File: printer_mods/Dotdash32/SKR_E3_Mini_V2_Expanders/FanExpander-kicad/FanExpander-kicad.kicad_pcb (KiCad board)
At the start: 2 copper layers, 46.3 x 37.3 mm, 69 parts, among them J0 FAN0, J1 FAN1, J10 FAN0_IN, J12 HI_PWR_IN, J2 FAN2, J3 FAN3, J4 FAN4, J5 FAN5, J6 FAN6, J7 FAN7, J8 EXP1_IN, J9 5V_In, Q1 IRLML6344, Q2 IRLML6344, Q3 IRLML6344, Q4 IRLML6344, Q5 IRLML6344, Q6 IRLML6344, Q7 IRLML6344

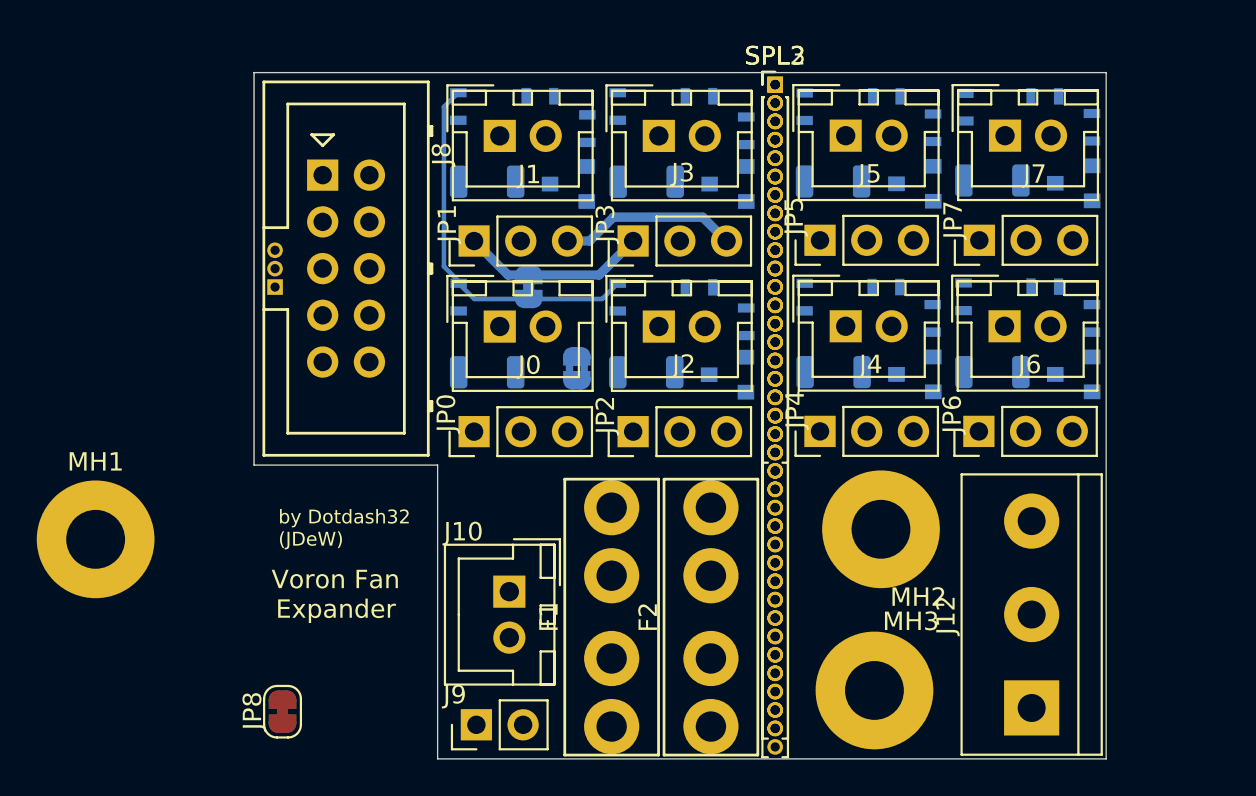
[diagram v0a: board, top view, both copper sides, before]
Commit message: feat: new layout with screw terminals and jumpers
add more jumpers to make any kind of voltage selection more easy,
particularly for fan0, either always on or cutting 24V in

no routing done yet lol
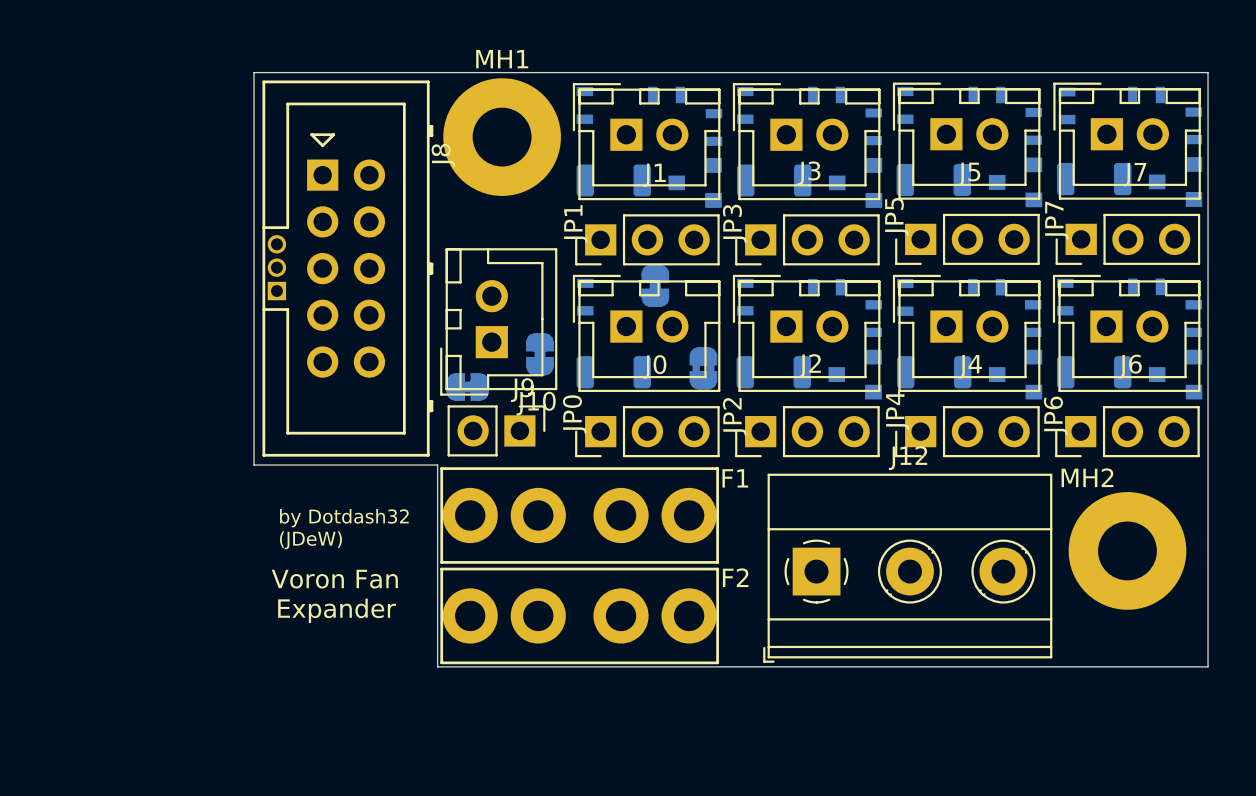
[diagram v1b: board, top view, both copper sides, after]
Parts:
- removed MH3: MountingHole, Mounting_Holes:MountingHole_3.2mm_M3_Pad
- removed SPL1: Fans 4-7, Pin_Headers:Pin_Header_Straight_1x21_Pitch1.00mm
- removed SPL2: Conn_01x37, Pin_Headers:Pin_Header_Straight_1x37_Pitch1.00mm
- removed SPL3: Conn_01x36, Pin_Headers:Pin_Header_Straight_1x36_Pitch1.00mm
- added JP11: Fan0_PWR, Jumper:SolderJumper-2_P1.3mm_Bridged_RoundedPad1.0x1.5mm, B.Cu at (52.1, 61.9)
- F1, F2: value Polyfuse-2.5A -> ATM-Fuse
- J12: value HI_PWR_IN -> HI_PWR2; footprint Connectors_Terminal_Blocks:TerminalBlock_bornier-3_P5.08mm -> TerminalBlock_Pheonix:TerminalBlock_Phoenix_MKDS-1,5-3-5.08_1x03_P5.08mm_Horizontal
- JP10: footprint Pin_Headers:Pin_Header_Straight_1x03_Pitch1.00mm -> Pin_Headers:Pin_Header_Straight_1x03_Pitch1.27mm
- JP8: moved to B.Cu
- moved MH1 31.1 mm to (50.0, 50.1)
- moved JP8 20.3 mm to (48.2, 63.7), turned to 0 degrees
- moved J9 16.2 mm to (51.0, 66.1), turned to 270 degrees
- moved J12 13.8 mm to (67.1, 73.7), turned to 0 degrees
- moved J10 13.6 mm to (49.5, 61.2), turned to 90 degrees
- moved MH2 13.5 mm to (84.0, 72.6)
- moved F2 7.14 mm to (54.3, 76.1), turned to 180 degrees
- moved R7 6.94 mm to (70.2, 49.5)
- moved R6 6.94 mm to (70.2, 60.0)
- moved D5 6.93 mm to (64.8, 52.5)
- moved JP3 6.93 mm to (64.1, 55.7)
- moved Q3 6.93 mm to (69.3, 52.6)
- moved J3 6.93 mm to (65.5, 50.0)
- moved R3 6.93 mm to (63.3, 48.4)
- moved R11 6.93 mm to (67.7, 47.8)
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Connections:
- J10 pad 1: /24V_unFused -> /24V_F0
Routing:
- net /LED_Drive: track 20.4 -> 0.00 mm
- net +5V: track 10.2 -> 0.00 mm
- net +24V: track 9.73 -> 0.00 mm
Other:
- board size 46.3 x 37.3 mm -> 51.9 x 32.3 mm

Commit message: chore: updating layout to new method, new LED
new LED reverse mount footprint, should be slightly less bulky
and make sure all the light just goes up through JST connector
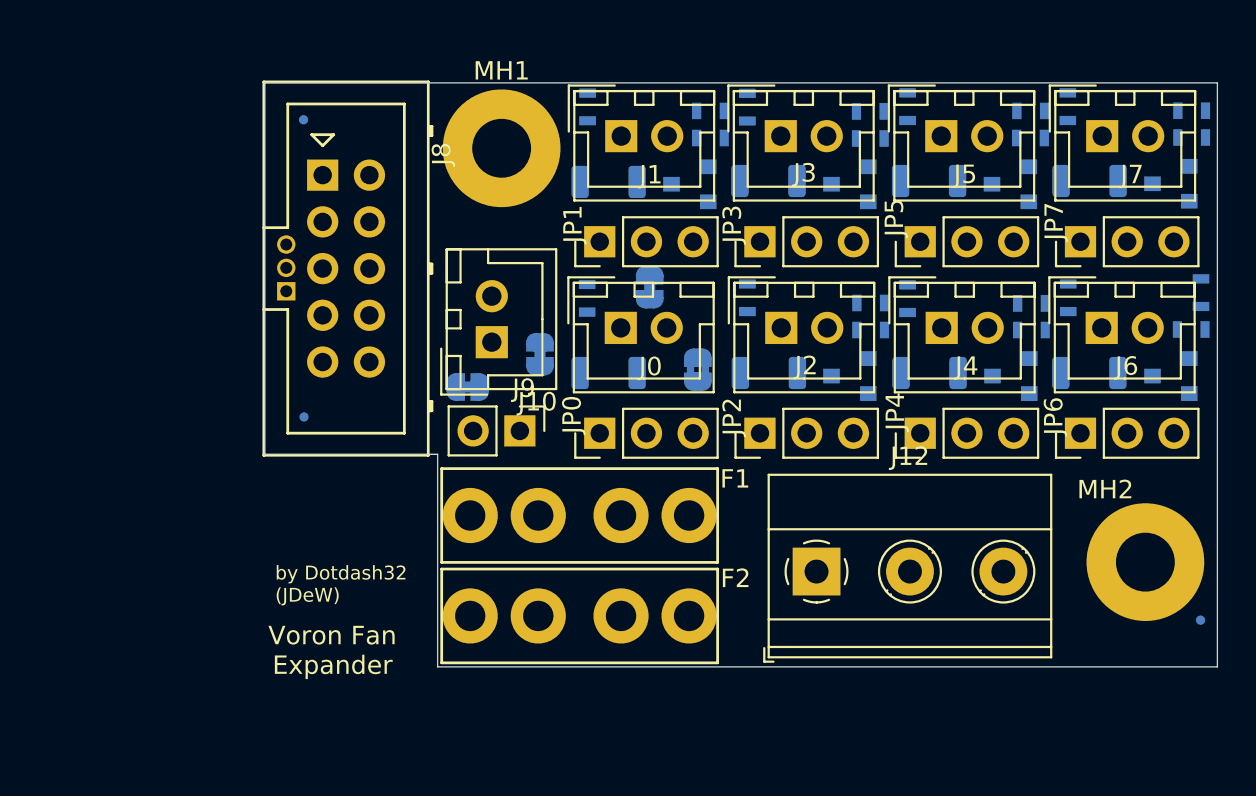
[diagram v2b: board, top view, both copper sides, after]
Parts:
- added FID1: Fiducial, Fiducials:Fiducial_0.5mm_Dia_1mm_Outer, B.Cu at (39.2, 49.1)
- added FID2: Fiducial, Fiducials:Fiducial_0.5mm_Dia_1mm_Outer, B.Cu at (39.3, 65.3)
- added FID3: Fiducial, Fiducials:Fiducial_0.5mm_Dia_1mm_Outer, B.Cu at (88.0, 76.4)
- moved R21 3.37 mm to (87.5, 50.1)
- moved R12 3.37 mm to (78.8, 60.6)
- moved R20 3.36 mm to (87.5, 60.6)
- moved R11 3.35 mm to (70.1, 50.2)
- moved R10 3.34 mm to (70.1, 60.6)
- moved R9 3.34 mm to (61.4, 50.1)
- moved R19 3.32 mm to (78.8, 50.1)
- moved R17 1.46 mm to (88.0, 58.5), turned to 270 degrees
- moved MH2 1.15 mm to (85.0, 73.2)
- moved R5 0.92 mm to (61.4, 48.7), turned to 180 degrees
- moved R6 0.87 mm to (70.1, 59.1), turned to 0 degrees
- moved R7 0.86 mm to (70.1, 48.7), turned to 0 degrees
- moved R16 0.85 mm to (78.8, 48.7), turned to 0 degrees
- moved R18 0.83 mm to (87.5, 48.7), turned to 0 degrees
- moved R8 0.83 mm to (78.8, 59.1), turned to 0 degrees
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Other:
- board size 51.9 x 32.3 mm -> 51.8 x 31.7 mm

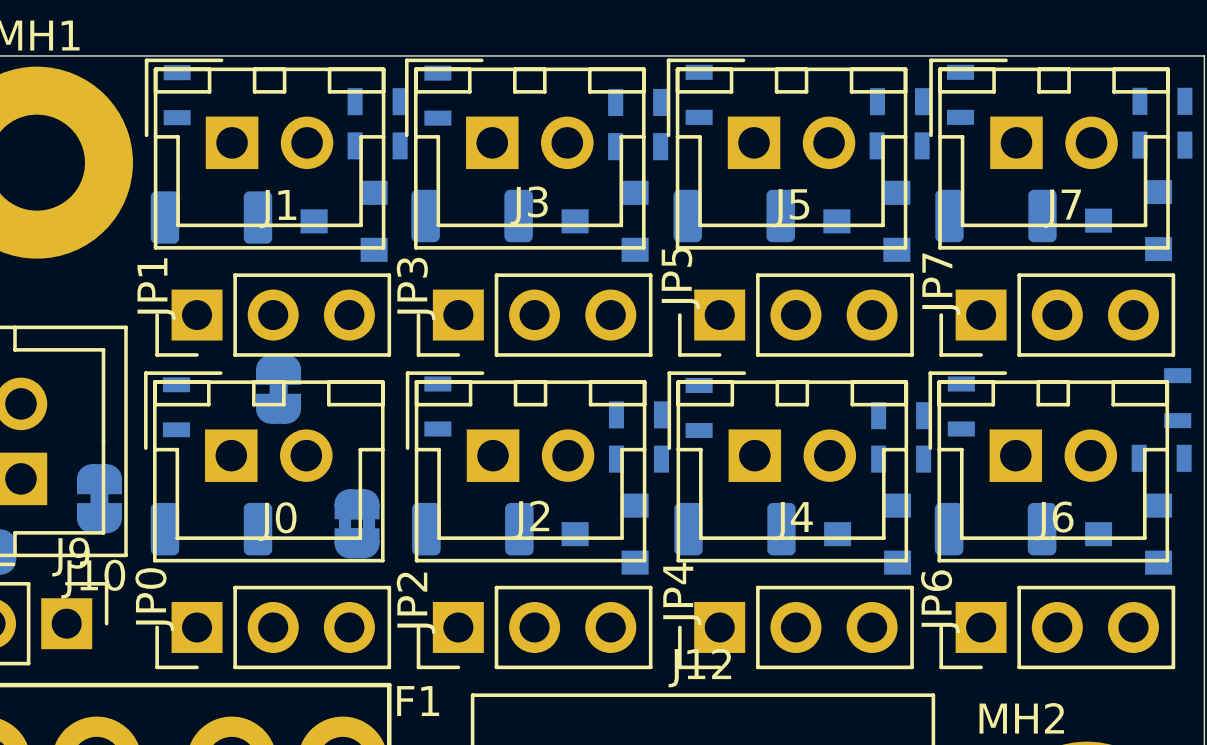
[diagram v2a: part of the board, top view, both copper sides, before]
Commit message: chore: changing values for BOM export
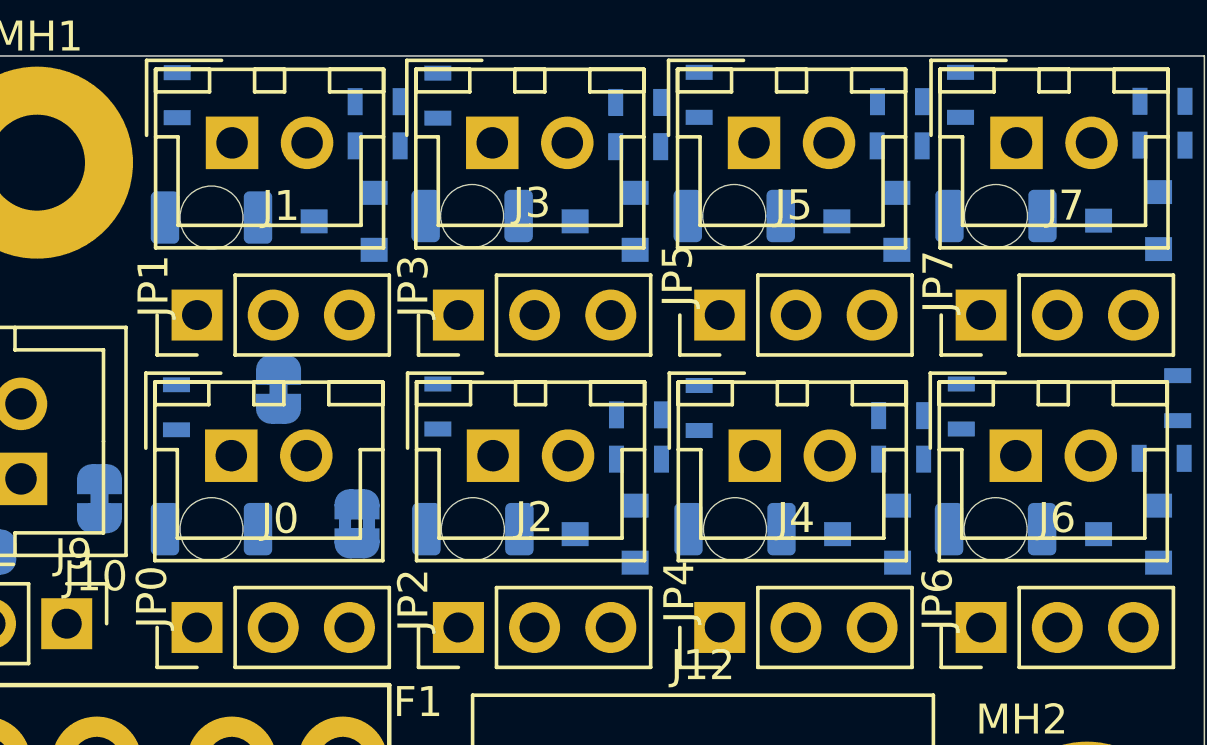
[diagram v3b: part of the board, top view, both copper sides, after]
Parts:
- D1, D2, D3, D4, D5, D6, D7, D8: footprint LED_SMD:LED_1206_3216Metric_ReverseMount_Hole1.8x2.4mm -> LED_SMD:LED_1206_3216Metric_ReverseMount_Hole2.1x2.1mm
- J0: value FAN0 -> JST-XH2
- J1: value FAN1 -> JST-XH2
- J10: value FAN0_IN -> JST-XH2
- J2: value FAN2 -> JST-XH2
- J3: value FAN3 -> JST-XH2
- J4: value FAN4 -> JST-XH2
- J5: value FAN5 -> JST-XH2
- J6: value FAN6 -> JST-XH2
- J7: value FAN7 -> JST-XH2
- J8: value EXP1_IN -> EXPx_IN
- JP0: value V_SELECT0 -> V_SELECT
- JP1: value V_SELECT1 -> V_SELECT
- JP2: value V_SELECT2 -> V_SELECT
- JP3: value V_SELECT3 -> V_SELECT
- JP4: value V_SELECT4 -> V_SELECT
- JP5: value V_SELECT5 -> V_SELECT
- JP6: value V_SELECT6 -> V_SELECT
- JP7: value V_SELECT7 -> V_SELECT

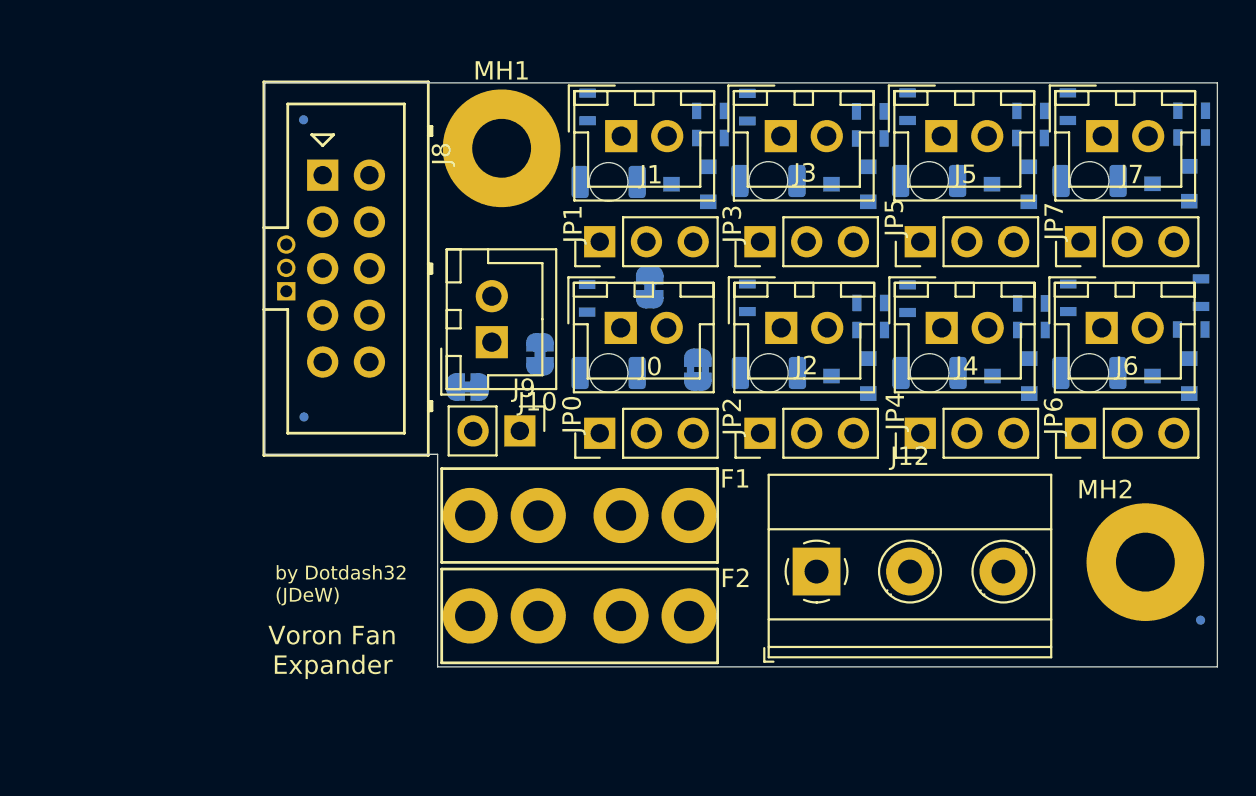
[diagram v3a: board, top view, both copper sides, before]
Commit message: feat: initial routing of FE beefy boi
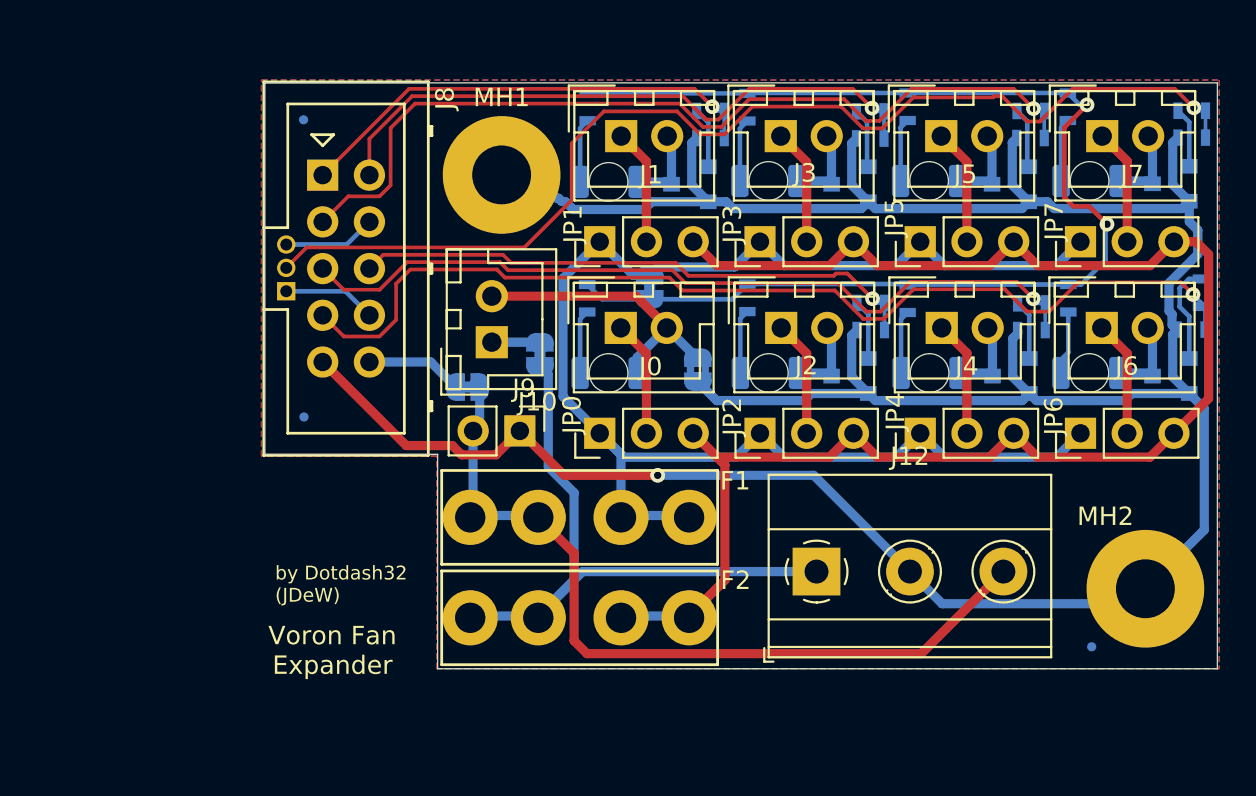
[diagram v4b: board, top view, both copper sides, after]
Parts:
- moved FID3 6.09 mm to (82.1, 77.8)
- moved MH1 1.45 mm to (50.0, 52.1)
- moved MH2 1.45 mm to (85.0, 74.6)
- moved F1 0.10 mm to (54.3, 70.8)
- moved F2 0.10 mm to (54.3, 76.2)
- turned R5 to 0 degrees
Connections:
- J8 pad 1: /FAN4 -> /FAN1
- J8 pad 2: /FAN6 -> /FAN3
- J8 pad 3: /FAN2 -> /FAN5
- J8 pad 5: /FAN1 -> /FAN4
- J8 pad 6: /FAN5 -> /FAN2
- J8 pad 7: /FAN3 -> /FAN6
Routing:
- net GND: track 0.00 -> 166.8 mm, vias 0 -> 1
- net +24V: track 0.00 -> 86.6 mm
- net +5V: track 0.00 -> 79.9 mm
- net /LED_Drive: track 0.00 -> 67.3 mm, vias 0 -> 2
- net /FAN7: track 0.00 -> 60.9 mm, vias 0 -> 1
- net /FAN6: track 0.00 -> 55.8 mm, vias 0 -> 1
- net /FAN5: track 0.00 -> 48.1 mm, vias 0 -> 1
- net /FAN4: track 0.00 -> 44.1 mm, vias 0 -> 1
- net /5V_unFused: track 0.00 -> 43.9 mm
- net /24V_unFused: track 0.00 -> 35.0 mm
- net /FAN3: track 0.00 -> 34.1 mm, vias 0 -> 1
- net /FAN2: track 0.00 -> 31.0 mm, vias 0 -> 1
- net /FAN1: track 0.00 -> 25.7 mm, vias 0 -> 1
- net /FAN0_Dr: track 0.00 -> 15.7 mm
- net /F3V: track 0.00 -> 6.32 mm
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- added copper zone on B.Cu, net GND
- added copper zone on F.Cu, net GND
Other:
- board size 51.8 x 31.7 mm -> 51.8 x 31.9 mm

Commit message: feat: pcb corner fillets, silk layout
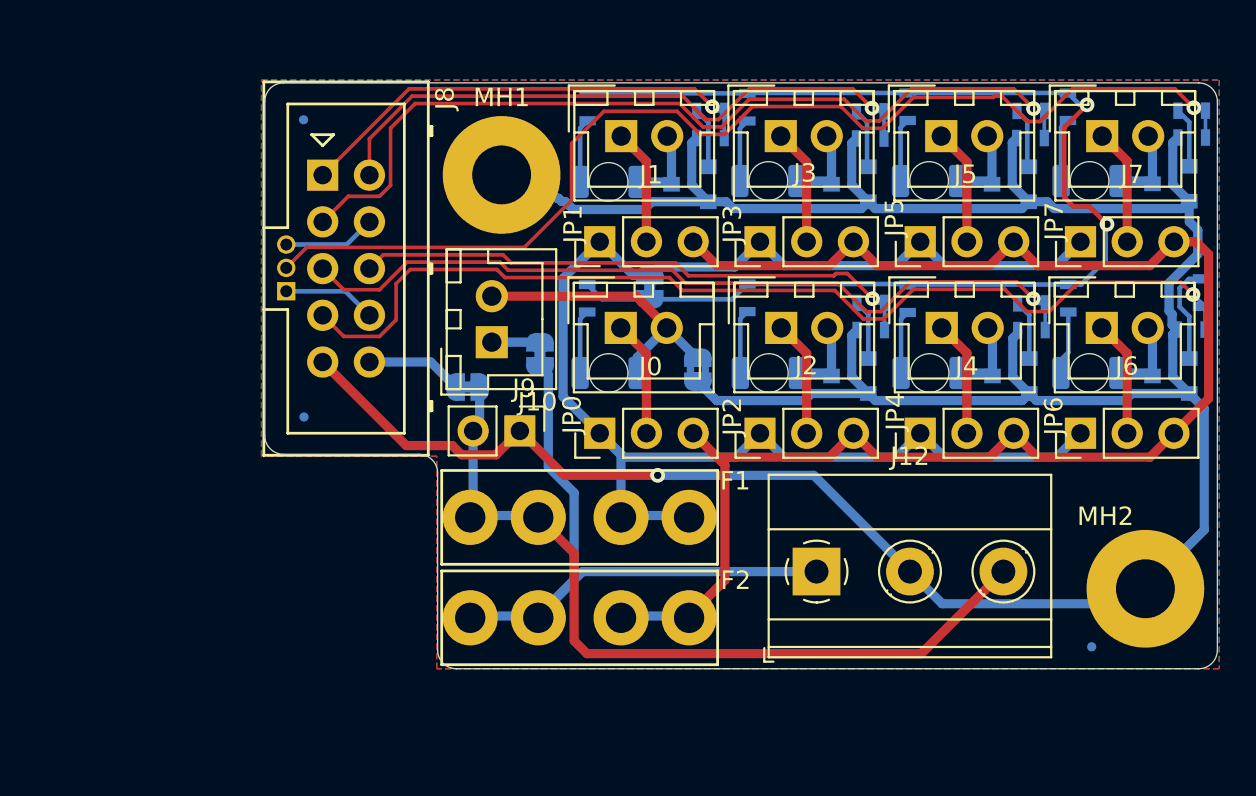
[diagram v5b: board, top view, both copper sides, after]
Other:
- outline, holes or cut-outs redrawn
- board text added: "EXP Choose"
- board text added: "JLCJLCJLCJLC"
- board text added: "Voron Fan Expander Big Beefy Boi V0.1.5"
- board text removed: "Voron Fan Expander"

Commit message: feat: prep big expander for release
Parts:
- added JP13: 5V_Term, Jumper:SolderJumper-2_P1.3mm_Open_RoundedPad1.0x1.5mm, B.Cu at (76.6, 70.6)
- added JP14: 24V_Term, Jumper:SolderJumper-2_P1.3mm_Open_RoundedPad1.0x1.5mm, B.Cu at (66.5, 70.6)
- JP11, JP8, JP9: footprint Jumper:SolderJumper-2_P1.3mm_Bridged_RoundedPad1.0x1.5mm -> Jumper:SolderJumper-2_P1.3mm_Pasted_RoundedPad1.0x1.5mm
- JP12: footprint Jumper:SolderJumper-2_P1.3mm_Bridged2Bar_RoundedPad1.0x1.5mm -> Jumper:SolderJumper-2_P1.3mm_Open_RoundedPad1.0x1.5mm
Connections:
- J12 pad 1: /24V_unFused -> /24v_Screw
- J12 pad 3: /5V_unFused -> /5V_Screw
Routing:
- net /5V_Screw: track 0.00 -> 3.10 mm
- net /24v_Screw: track 0.00 -> 3.10 mm
- net /5V_unFused: track 43.9 -> 44.5 mm, vias 0 -> 1
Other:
- board text added: "Voron Fan Expander Big Beefy Boi V1.0.1"
- board text added: "by (JDeW) Dotdash32"
- board text removed: "Voron Fan Expander Big Beefy Boi V0.1.5"
- board text removed: "by Dotdash32 (JDeW)"
